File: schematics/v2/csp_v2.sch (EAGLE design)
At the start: 61 parts, among them IC1 74AHC1G08DCK, IC2 74HCT04D, IC3 PCA9555PW, IC4 LM339D, J1 2X20-CHIP2X20-SMT-CHIP, U2 DS2431P

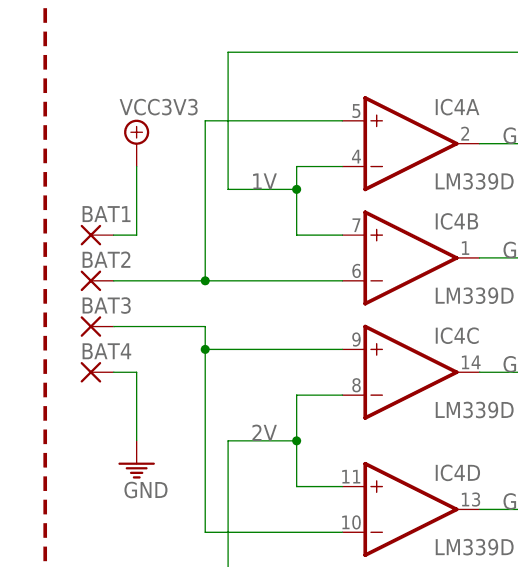
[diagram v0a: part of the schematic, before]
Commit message: updated layout
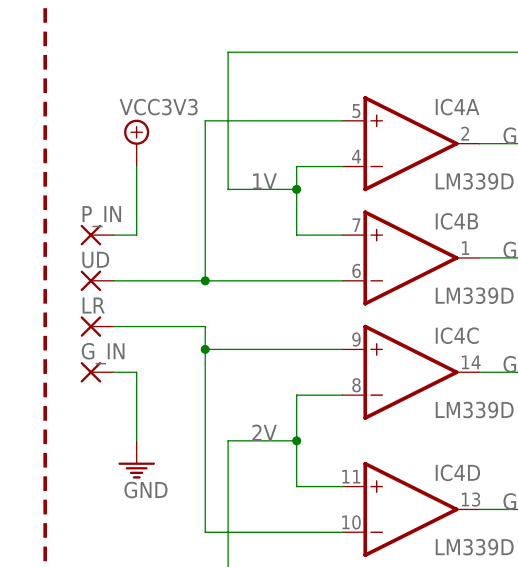
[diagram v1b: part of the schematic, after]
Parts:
- removed BAT1, BAT2, BAT3, BAT4: BTN, wirepad:SMD2
- added G_IN, LR, P_IN, UD: BTN, JKW_CHIP:SMD1.36X3
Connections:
- net GND: now also G_IN.P; no longer BAT4.P
- net N$30: now also UD.P; no longer BAT2.P
- net N$31: now also LR.P; no longer BAT3.P
- net VCC3V3: now also P_IN.P; no longer BAT1.P
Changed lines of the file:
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@@
 <?xml version="1.0" encoding="utf-8"?>
 <!DOCTYPE eagle SYSTEM "eagle.dtd">
-<eagle version="7.6.0">
+<eagle version="7.7.0">
 <drawing>
 <settings>
@@
 <part name="R3" library="rcl" deviceset="R-EU_" device="M0805" value="20k "/>
 <part name="R9" library="rcl" deviceset="R-EU_" device="M0805" value="10k "/>
-<part name="BAT1" library="wirepad" deviceset="SMD2" device="" value="BTN"/>
-<part name="BAT2" library="wirepad" deviceset="SMD2" device="" value="BTN"/>
-<part name="BAT3" library="wirepad" deviceset="SMD2" device="" value="BTN"/>
-<part name="BAT4" library="wirepad" deviceset="SMD2" device="" value="BTN"/>
+<part name="P_IN" library="JKW_CHIP" deviceset="SMD1.36X3" device="" value="BTN"/>
+<part name="UD" library="JKW_CHIP" deviceset="SMD1.36X3" device="" value="BTN"/>
+<part name="LR" library="JKW_CHIP" deviceset="SMD1.36X3" device="" value="BTN"/>
+<part name="G_IN" library="JKW_CHIP" deviceset="SMD1.36X3" device="" value="BTN"/>
 <part name="SUPPLY9" library="Keyboard v0.3" deviceset="VCC3V3" device=""/>
 <part name="U$22" library="Keyboard v0.2" deviceset="GND" device=""/>
@@
 <attribute name="VALUE" x="306.578" y="212.09" size="1.778" layer="96" rot="R270"/>
 </instance>
-<instance part="BAT1" gate="1" x="238.76" y="200.66" smashed="yes" rot="MR180">
+<instance part="P_IN" gate="1" x="238.76" y="200.66" smashed="yes" rot="MR180">
 <attribute name="NAME" x="237.617" y="203.8858" size="1.778" layer="95" rot="MR180"/>
 </instance>
-<instance part="BAT2" gate="1" x="238.76" y="195.58" smashed="yes" rot="MR180">
+<instance part="UD" gate="1" x="238.76" y="195.58" smashed="yes" rot="MR180">
 <attribute name="NAME" x="237.617" y="198.8058" size="1.778" layer="95" rot="MR180"/>
 </instance>
-<instance part="BAT3" gate="1" x="238.76" y="190.5" smashed="yes" rot="MR180">
+<instance part="LR" gate="1" x="238.76" y="190.5" smashed="yes" rot="MR180">
 <attribute name="NAME" x="237.617" y="193.7258" size="1.778" layer="95" rot="MR180"/>
 </instance>
-<instance part="BAT4" gate="1" x="238.76" y="185.42" smashed="yes" rot="MR180">
+<instance part="G_IN" gate="1" x="238.76" y="185.42" smashed="yes" rot="MR180">
 <attribute name="NAME" x="237.617" y="188.6458" size="1.778" layer="95" rot="MR180"/>
 </instance>
@@
 </segment>
 <segment>
-<pinref part="BAT4" gate="1" pin="P"/>
+<pinref part="G_IN" gate="1" pin="P"/>
 <wire x1="241.3" y1="185.42" x2="243.84" y2="185.42" width="0.1524" layer="91"/>
 <wire x1="243.84" y1="185.42" x2="243.84" y2="177.8" width="0.1524" layer="91"/>
@@
 </segment>
 <segment>
-<pinref part="BAT1" gate="1" pin="P"/>
+<pinref part="P_IN" gate="1" pin="P"/>
 <wire x1="241.3" y1="200.66" x2="243.84" y2="200.66" width="0.1524" layer="91"/>
 <wire x1="243.84" y1="200.66" x2="243.84" y2="208.28" width="0.1524" layer="91"/>
@@
 <net name="N$30" class="0">
 <segment>
-<pinref part="BAT2" gate="1" pin="P"/>
+<pinref part="UD" gate="1" pin="P"/>
 <wire x1="241.3" y1="195.58" x2="251.46" y2="195.58" width="0.1524" layer="91"/>
 <wire x1="251.46" y1="195.58" x2="251.46" y2="213.36" width="0.1524" layer="91"/>
@@
 <net name="N$31" class="0">
 <segment>
-<pinref part="BAT3" gate="1" pin="P"/>
+<pinref part="LR" gate="1" pin="P"/>
 <wire x1="241.3" y1="190.5" x2="251.46" y2="190.5" width="0.1524" layer="91"/>
 <wire x1="251.46" y1="190.5" x2="251.46" y2="187.96" width="0.1524" layer="91"/>
